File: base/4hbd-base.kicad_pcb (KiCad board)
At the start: 2 copper layers, 120 x 100 mm, 233 parts, among them J1 Spring_Terminal_Connector_01x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, J10 Spring_Terminal_Connector_01x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, J11 Spring_Terminal_Connector_01x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, J12 Spring_Terminal_Connector_01x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, J13 Screw_Terminal_01x02, J14 Conn_02x25_Odd_Even, J15 Conn_02x25_Odd_Even, J2 Spring_Terminal_Connector_01x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, J3 Spring_Terminal_Connector_01x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, J4 Spring_Terminal_Connector_01x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, J5 Spring_Terminal_Connector_01x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, J6 Spring_Terminal_Connector_01x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, J7 Screw_Terminal_01x03, J8 Screw_Terminal_01x04, J9 Spring_Terminal_Connector_01x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, Q1 irf540n, Q10 2N7002, Q11 2N7002, Q12 IRLML2060TRPBF, Q2 irf540n, Q3 irf540n, Q4 irf540n, Q5 irf540n, Q6 irf540n, Q7 irf540n, Q8 irf540n, Q9 2N7002, U1 SI8640, U10 ADS7886, U11 MOCD217M, U12 MOCD217M, U13 MOCD217M, U14 AMS1117-5.0, U15 AMS1117-5.0, U16 LM2596S-ADJ, U17 AM26LV32, U18 LM2596S-ADJ, U19 AMS1117-5.0, U2 SI8640, U20 SN65HVD230, U21 MAX485CSA, U3 IR2181, U4 IR2181, U5 IR2181, U6 IR2181, U7 ACS712xLCTR-30A, U8 ACS712xLCTR-30A, U9 ADS7886

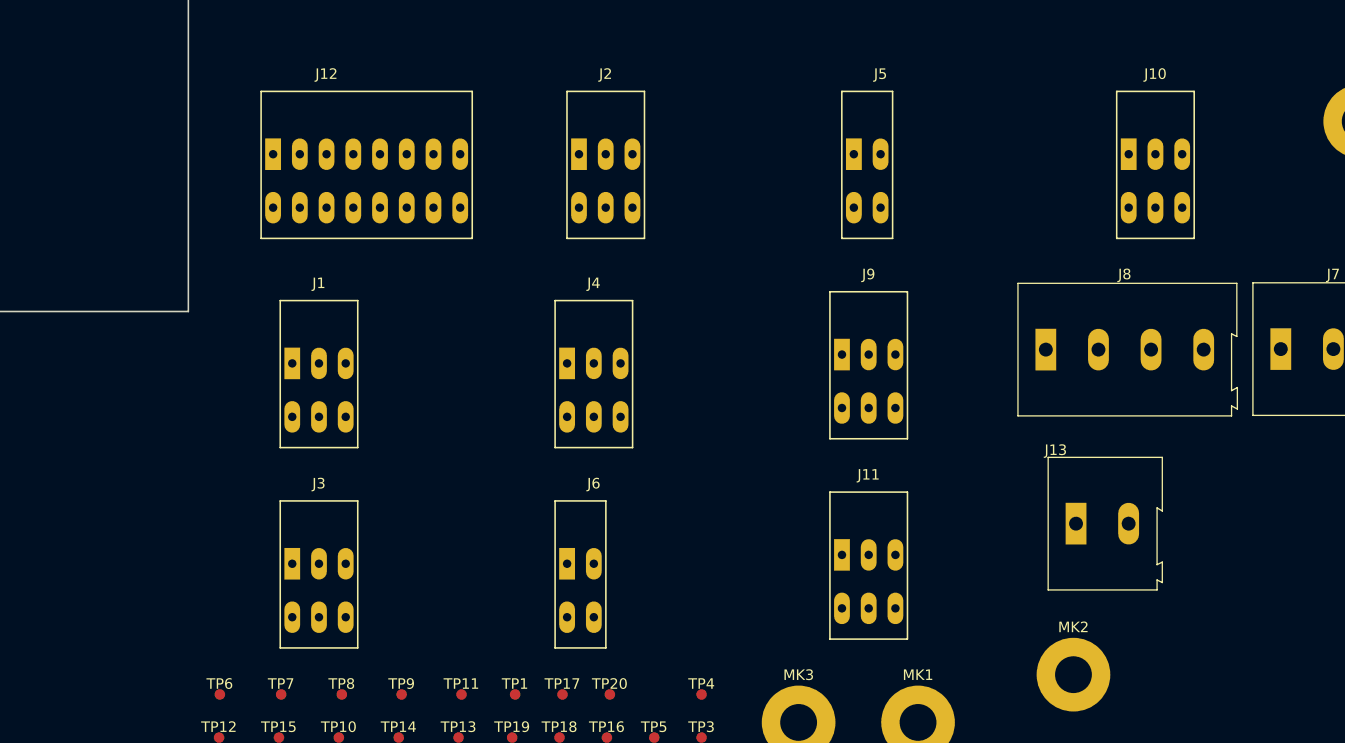
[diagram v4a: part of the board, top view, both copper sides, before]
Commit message: update pcb for TerminalBlock_KaiFeng footprint lib
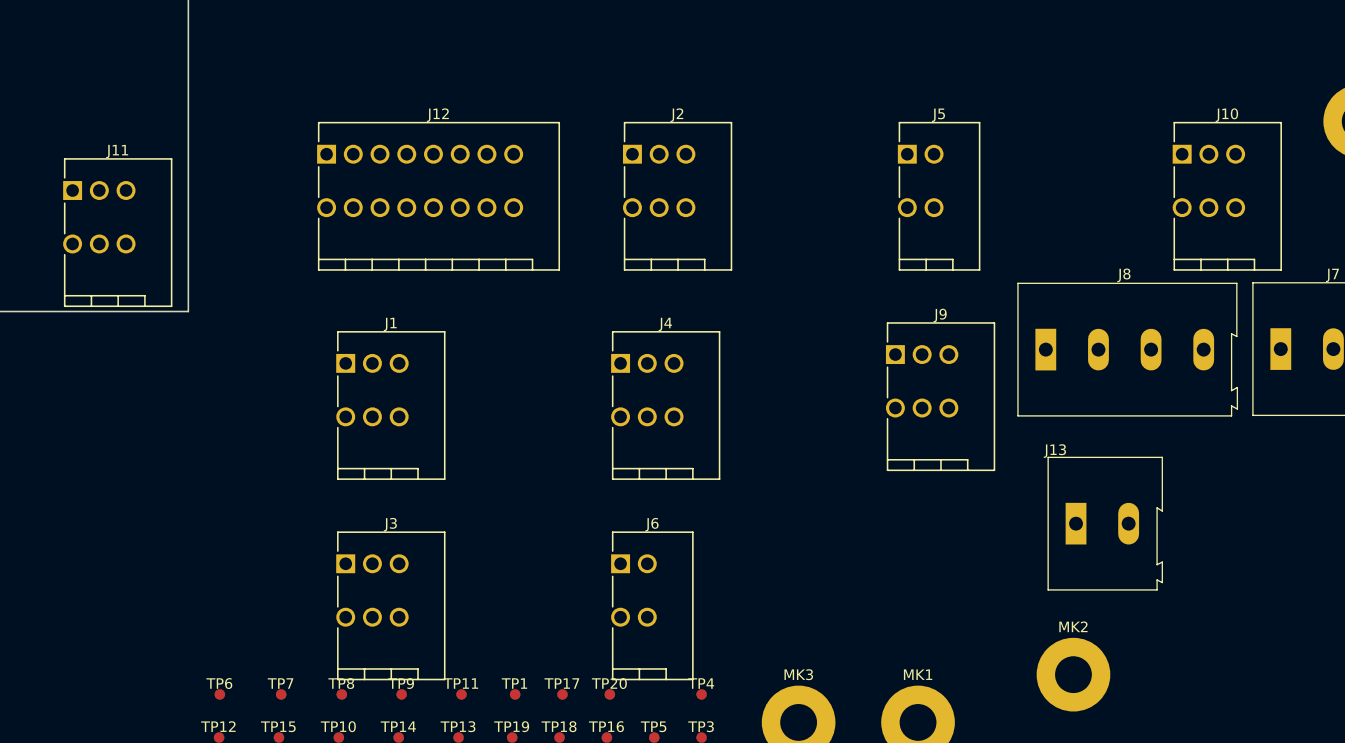
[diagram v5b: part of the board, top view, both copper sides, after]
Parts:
- J1, J10, J11, J2, J3, J4, J9: footprint TerminalBlock:SpringTerminalBlock_KF141R_3_P2.54mm -> TerminalBlock_KaiFeng:TerminalBlock_KaiFeng_KF141R-3_1x03_P2.54mm
- J12: footprint TerminalBlock:SpringTerminalBlock_KF141R_8_P2.54mm -> TerminalBlock_KaiFeng:TerminalBlock_KaiFeng_KF141R-8_1x08_P2.54mm
- J5, J6: footprint TerminalBlock:SpringTerminalBlock_KF141R_2_P2.54mm -> TerminalBlock_KaiFeng:TerminalBlock_KaiFeng_KF141R-2_1x02_P2.54mm
- moved J11 85.5 mm to (127.0, 120.5)

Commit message: update pcb
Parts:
- moved J10 203.9 mm to (29.0, 103.5)
- moved J9 185.8 mm to (20.0, 121.0)
- moved J8 179.3 mm to (42.5, 107.0)
- moved J7 179.2 mm to (65.0, 106.5)
- moved J5 173.9 mm to (32.5, 121.0)
- moved J6 168.0 mm to (19.5, 103.5)
- moved J13 147.6 mm to (82.0, 106.5)
- moved J3 114.4 mm to (44.0, 121.0)
- moved J1 94.8 mm to (59.5, 121.0)
- moved J2 77.8 mm to (102.5, 120.5)
- moved J12 76.2 mm to (75.0, 121.0)
- moved J4 65.2 mm to (116.0, 120.5)
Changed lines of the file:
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@@
   )
   (module TerminalBlock:TerminalBlock_Altech_AK300-3_P5.00mm placed (layer F.Cu)
-    (at 241.818573 135.569999)
+    (at 65 106.5)
     (descr "Altech AK300 terminal block, pitch 5.0mm, 45 degree angled, see http://www.mouser.com/ds/2/16/PCBMETRC-24178.pdf")
     (tags "Altech AK300 terminal block pitch 5.0mm")
@@
   )
   (module TerminalBlock:TerminalBlock_Altech_AK300-4_P5.00mm placed (layer F.Cu)
-    (at 219.490002 135.619999)
+    (at 42.5 107)
     (descr "Altech AK300 terminal block, pitch 5.0mm, 45 degree angled, see http://www.mouser.com/ds/2/16/PCBMETRC-24178.pdf")
     (tags "Altech AK300 terminal block pitch 5.0mm")
@@
   )
   (module TerminalBlock:TerminalBlock_Altech_AK300-2_P5.00mm (layer F.Cu)
-    (at 222.358573 152.159999)
+    (at 82 106.5)
     (descr "Altech AK300 terminal block, pitch 5.0mm, 45 degree angled, see http://www.mouser.com/ds/2/16/PCBMETRC-24178.pdf")
     (tags "Altech AK300 terminal block pitch 5.0mm")
@@
   )
   (module TerminalBlock_KaiFeng:TerminalBlock_KaiFeng_KF141R-3_1x03_P2.54mm (layer F.Cu)
-    (at 152.954357 136.929999)
+    (at 59.5 121)
     (descr "KaiFeng screwless terminal block, see http://www.nb-kaifeng.com/upload/file/1491789826.pdf")
     (tags "KF141R spring terminal block pitch 2.54mm")
@@
   )
   (module TerminalBlock_KaiFeng:TerminalBlock_KaiFeng_KF141R-3_1x03_P2.54mm (layer F.Cu)
-    (at 180.204357 117.049999)
+    (at 102.5 120.5)
     (descr "KaiFeng screwless terminal block, see http://www.nb-kaifeng.com/upload/file/1491789826.pdf")
     (tags "KF141R spring terminal block pitch 2.54mm")
@@
   )
   (module TerminalBlock_KaiFeng:TerminalBlock_KaiFeng_KF141R-3_1x03_P2.54mm (layer F.Cu)
-    (at 152.954357 155.969999)
+    (at 44 121)
     (descr "KaiFeng screwless terminal block, see http://www.nb-kaifeng.com/upload/file/1491789826.pdf")
     (tags "KF141R spring terminal block pitch 2.54mm")
@@
   )
   (module TerminalBlock_KaiFeng:TerminalBlock_KaiFeng_KF141R-3_1x03_P2.54mm (layer F.Cu)
-    (at 179.074357 136.929999)
+    (at 116 120.5)
     (descr "KaiFeng screwless terminal block, see http://www.nb-kaifeng.com/upload/file/1491789826.pdf")
     (tags "KF141R spring terminal block pitch 2.54mm")
@@
   )
   (module TerminalBlock_KaiFeng:TerminalBlock_KaiFeng_KF141R-2_1x02_P2.54mm (layer F.Cu)
-    (at 206.324357 117.049999)
+    (at 32.5 121)
     (descr "KaiFeng screwless terminal block, see http://www.nb-kaifeng.com/upload/file/1491789826.pdf")
     (tags "KF141R spring terminal block pitch 2.54mm")
@@
   )
   (module TerminalBlock_KaiFeng:TerminalBlock_KaiFeng_KF141R-2_1x02_P2.54mm (layer F.Cu)
-    (at 179.074357 155.969999)
+    (at 19.5 103.5)
     (descr "KaiFeng screwless terminal block, see http://www.nb-kaifeng.com/upload/file/1491789826.pdf")
     (tags "KF141R spring terminal block pitch 2.54mm")
@@
   )
   (module TerminalBlock_KaiFeng:TerminalBlock_KaiFeng_KF141R-3_1x03_P2.54mm (layer F.Cu)
-    (at 205.194357 136.089999)
+    (at 20 121)
     (descr "KaiFeng screwless terminal block, see http://www.nb-kaifeng.com/upload/file/1491789826.pdf")
     (tags "KF141R spring terminal block pitch 2.54mm")
@@
   )
   (module TerminalBlock_KaiFeng:TerminalBlock_KaiFeng_KF141R-3_1x03_P2.54mm (layer F.Cu)
-    (at 232.444357 117.049999)
+    (at 29 103.5)
     (descr "KaiFeng screwless terminal block, see http://www.nb-kaifeng.com/upload/file/1491789826.pdf")
     (tags "KF141R spring terminal block pitch 2.54mm")
@@
   )
   (module TerminalBlock_KaiFeng:TerminalBlock_KaiFeng_KF141R-8_1x08_P2.54mm (layer F.Cu)
-    (at 151.135717 117.049999)
+    (at 75 121)
     (descr "KaiFeng screwless terminal block, see http://www.nb-kaifeng.com/upload/file/1491789826.pdf")
     (tags "KF141R spring terminal block pitch 2.54mm")

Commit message: update fooprints for mosfet
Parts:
- Q1: footprint Package_TO_SOT_THT:TO-220-3_Horizontal -> Package_TO_SOT_THT:TO-220-3_TabUp
- Q2, Q3, Q4, Q5, Q6, Q7, Q8: footprint Package_TO_SOT_THT:TO-220-3_Vertical -> Package_TO_SOT_THT:TO-220-3_TabUp
- moved Q8 260.4 mm to (60.0, 76.0), turned to 270 degrees
- moved Q4 259.2 mm to (60.0, 52.0), turned to 270 degrees
- moved Q5 240.9 mm to (68.0, 69.0), turned to 90 degrees
- moved Q3 240.7 mm to (68.0, 57.0), turned to 90 degrees
- moved Q2 229.5 mm to (60.0, 40.0), turned to 270 degrees
- moved Q6 229.0 mm to (60.0, 64.0), turned to 270 degrees
- moved Q7 220.2 mm to (68.0, 81.0), turned to 90 degrees
- moved Q1 206.6 mm to (68.0, 45.0), turned to 90 degrees

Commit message: pcb was edited
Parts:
- moved R36 328.0 mm to (66.5, 112.5)
- moved R35 308.9 mm to (66.5, 87.8)
- moved L5 287.0 mm to (95.0, 164.8)
- moved U14 263.0 mm to (63.5, 15.5)
- moved R45 262.4 mm to (91.5, 17.2)
- moved C39 256.8 mm to (117.0, 165.2)
- moved C38 254.3 mm to (131.8, 137.5), turned to 270 degrees
- moved D26 253.5 mm to (101.0, 16.5)
- moved R46 252.2 mm to (95.0, 17.0)
- moved U18 235.4 mm to (118.5, 138.0)
- moved C35 229.4 mm to (124.2, 16.5)
- moved C40 221.6 mm to (131.5, 162.5), turned to 90 degrees
- moved D23 219.0 mm to (111.0, 74.0), turned to 90 degrees
- moved C24 212.9 mm to (115.5, 77.8)
- moved D24 212.2 mm to (125.2, 74.2), turned to 90 degrees
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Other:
- board size 120 x 100 mm -> 182 x 100 mm
